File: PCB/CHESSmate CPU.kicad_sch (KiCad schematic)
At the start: 3 parts, among them J1 Conn_01x22_Pin, J2 Conn_01x02_Pin, U1 ESP32-DEVKITC-32D

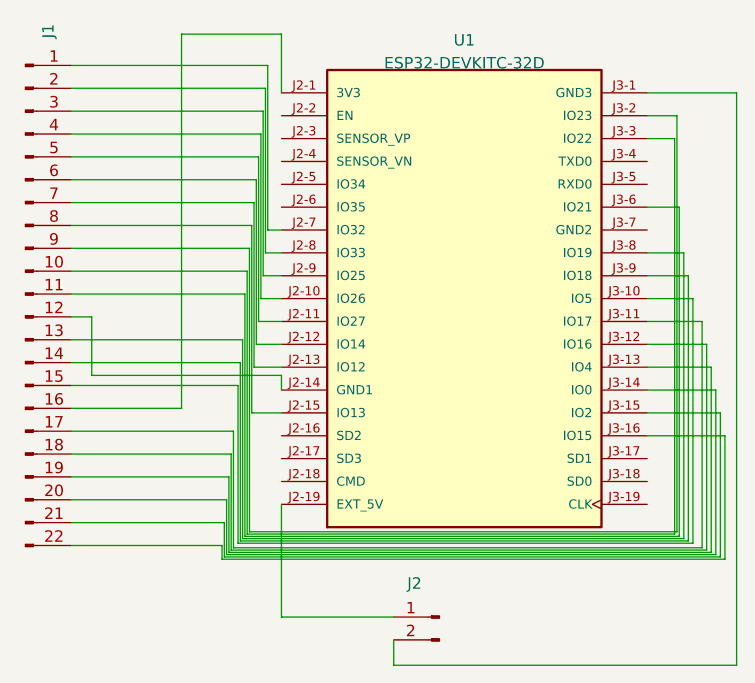
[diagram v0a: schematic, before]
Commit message: 23 pin CPU connector
This doesn't work because you can't use GPIO6, so I designed a new CPU board with a Pi Pico
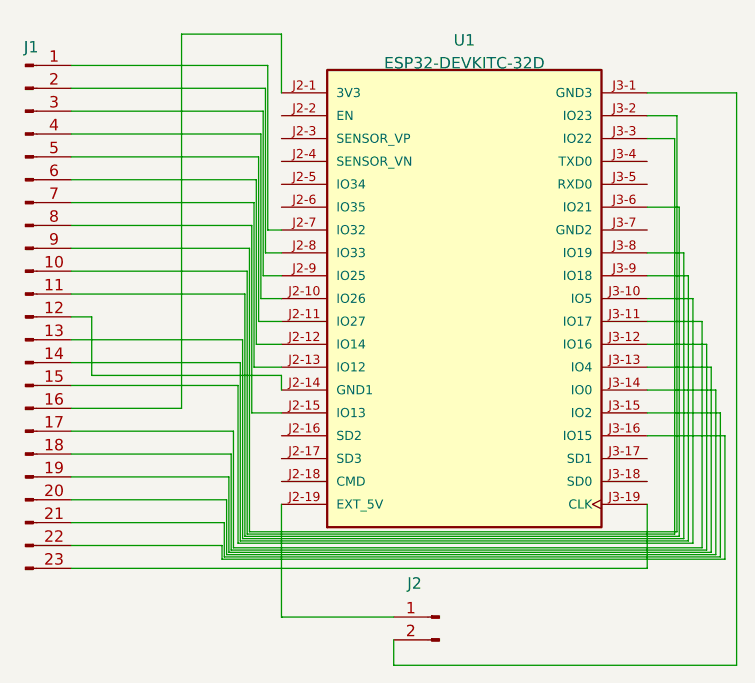
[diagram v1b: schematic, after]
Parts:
- J1: footprint Connector_PinHeader_2.54mm:PinHeader_1x22_P2.54mm_Vertical -> Connector_PinHeader_2.54mm:PinHeader_1x23_P2.54mm_Vertical; symbol Connector:Conn_01x22_Pin -> Connector:Conn_01x23_Pin
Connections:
- net at U1.J3-19 (CLK): now also J1.23 (Pin_23)
